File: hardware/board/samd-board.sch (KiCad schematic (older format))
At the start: 23 parts, among them J1 USB_B_Mini, J2 Conn_ARM_JTAG_SWD_10, J3 Conn_01x16_Male, J4 Conn_01x16_Male, SW1 SW_Push, U1 AZ1117-3.3, U2 ATSAMD21E17D-A, Y1 8MHz

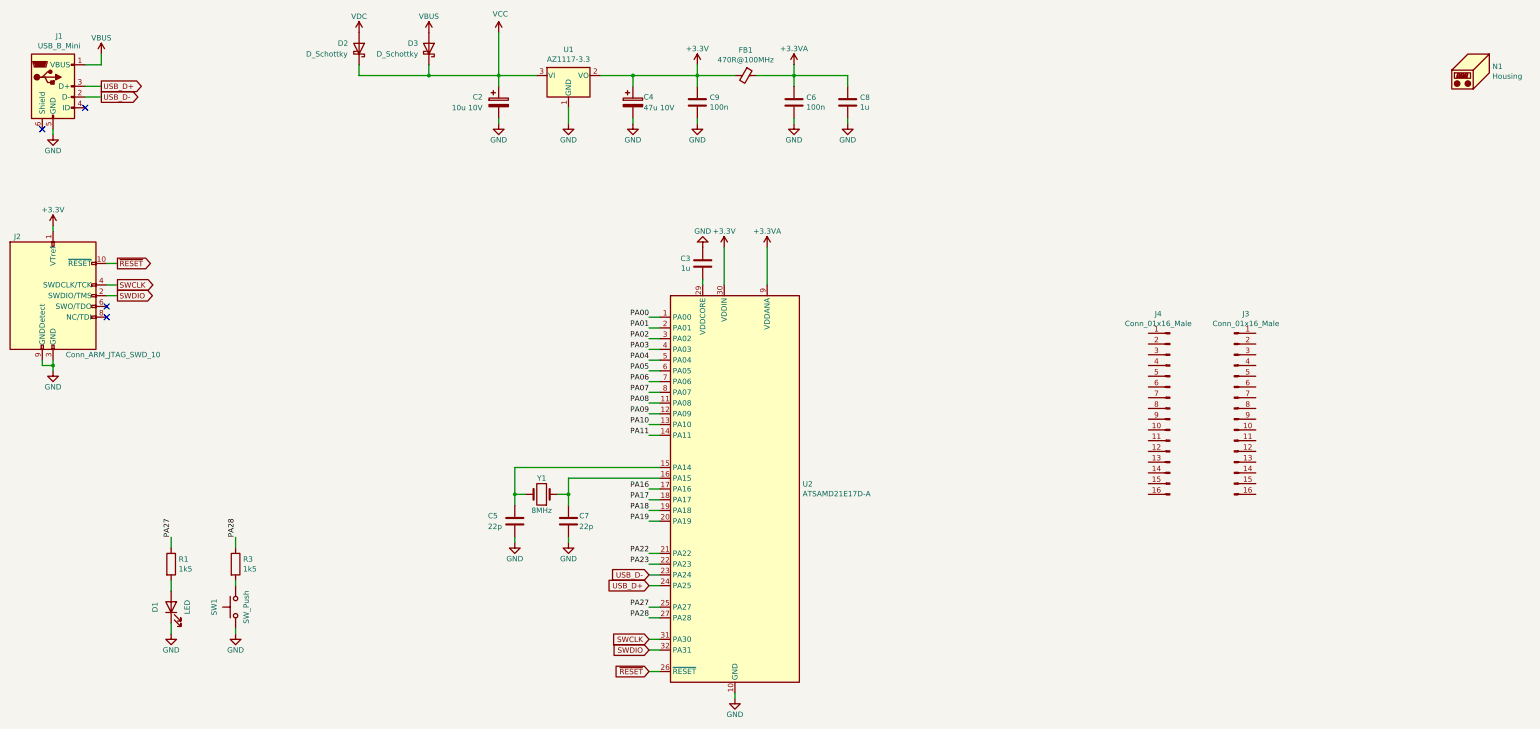
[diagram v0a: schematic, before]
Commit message: complete basic routing
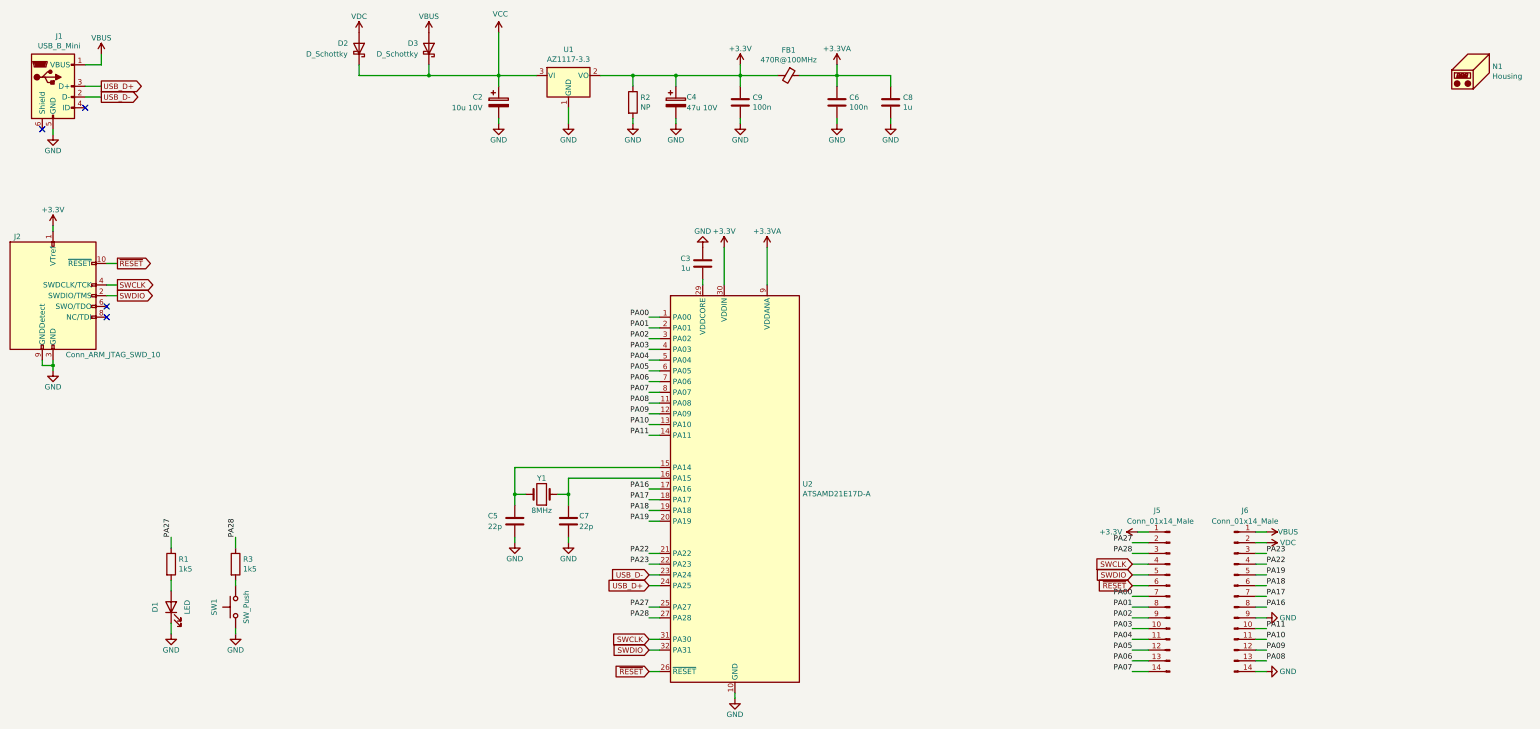
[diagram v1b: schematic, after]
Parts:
- removed J3, J4: Conn_01x16_Male, Connector_PinHeader_2.54mm:PinHeader_1x16_P2.54mm_Vertical, symbol Connector:Conn_01x16_Male
- added J5, J6: Conn_01x14_Male, Connector_PinHeader_2.54mm:PinHeader_1x14_P2.54mm_Vertical, symbol Connector:Conn_01x14_Male
- added R2: NP, Resistor_SMD:R_0603_1608Metric_Pad0.98x0.95mm_HandSolder, symbol Device:R
- J1: footprint Connector_USB:USB_Micro-B_Wuerth_629105150521 -> Assorted:USB_Micro-B_Wuerth_629105150521
- Y1: footprint Crystal:Crystal_SMD_5032-2Pin_5.0x3.2mm_HandSoldering -> Assorted:Crystal_SMD_Abracon_ABM3-2Pin_5.0x3.2mm
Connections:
- net +3V3: now also J5.1 (Pin_1), R2.1
- net GND: now also J6.14 (Pin_14), J6.9 (Pin_9), R2.2
- net PA00: now also J5.7 (Pin_7)
- net PA01: now also J5.8 (Pin_8)
- net PA02: now also J5.9 (Pin_9)
- net PA03: now also J5.10 (Pin_10)
- net PA04: now also J5.11 (Pin_11)
- net PA05: now also J5.12 (Pin_12)
- net PA06: now also J5.13 (Pin_13)
- net PA07: now also J5.14 (Pin_14)
- net PA08: now also J6.13 (Pin_13)
- net PA09: now also J6.12 (Pin_12)
- net PA10: now also J6.11 (Pin_11)
- net PA11: now also J6.10 (Pin_10)
- net PA16: now also J6.8 (Pin_8)
- net PA17: now also J6.7 (Pin_7)
- net PA18: now also J6.6 (Pin_6)
- net PA19: now also J6.5 (Pin_5)
- net PA22: now also J6.4 (Pin_4)
- net PA23: now also J6.3 (Pin_3)
- net PA27: now also J5.2 (Pin_2)
- net PA28: now also J5.3 (Pin_3)
- net SWCLK: now also J5.4 (Pin_4)
- net SWDIO: now also J5.5 (Pin_5)
- net VBUS: now also J6.1 (Pin_1)
- net VDC: now also J6.2 (Pin_2)
- net ~RESET: now also J5.6 (Pin_6)
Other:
- moved on the sheet: C4, C6, C8, C9, FB1
